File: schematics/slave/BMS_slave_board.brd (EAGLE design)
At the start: 75.9 x 50.8 mm, 73 parts, among them IC1 78L05F, IC2 ATTINY87/167AUTOMOTIVESOIC, IC3 LT1021S, IC4 78L05F, J1 AVR_SPI_PRG_6NS, Q1 BSS123, Q2 BSS123, Q3 BSS123, Q4 BSS123, U1 LMV324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

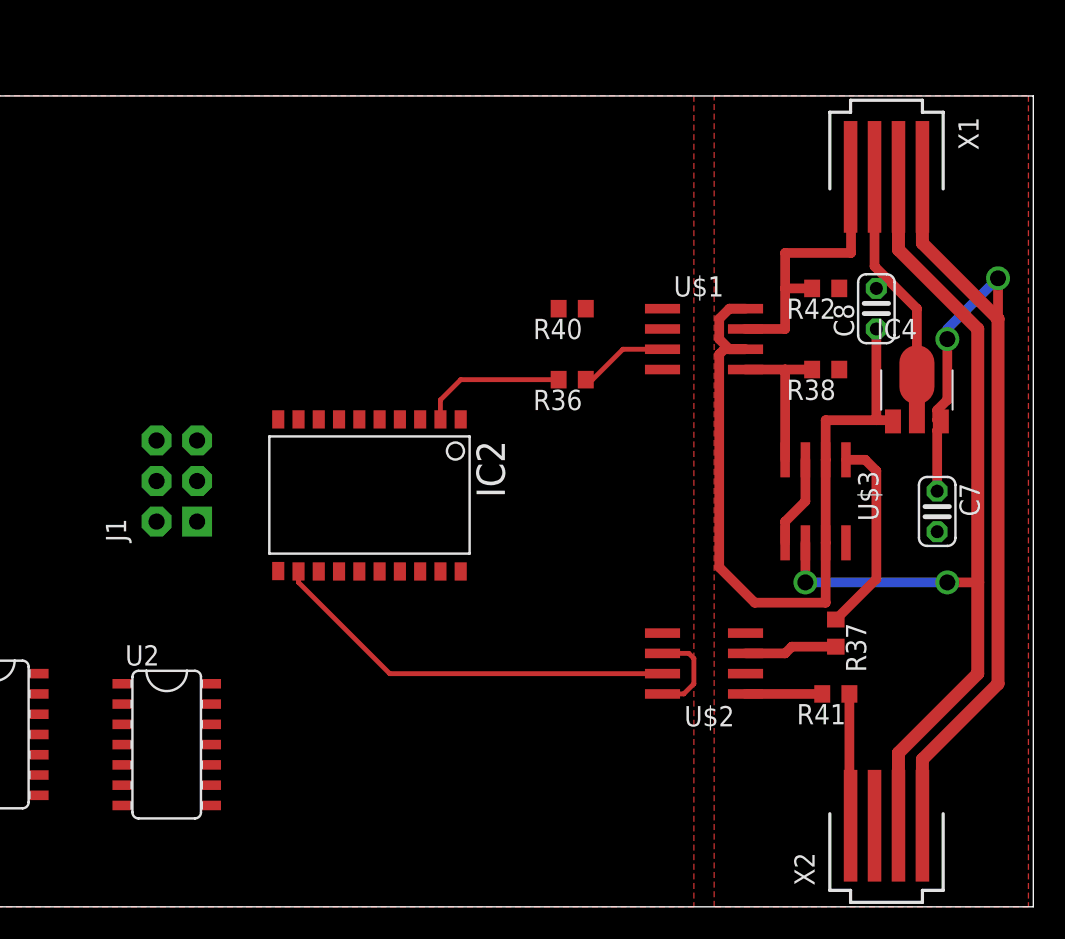
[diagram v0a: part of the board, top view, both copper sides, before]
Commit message: worked on ground plane and power pour
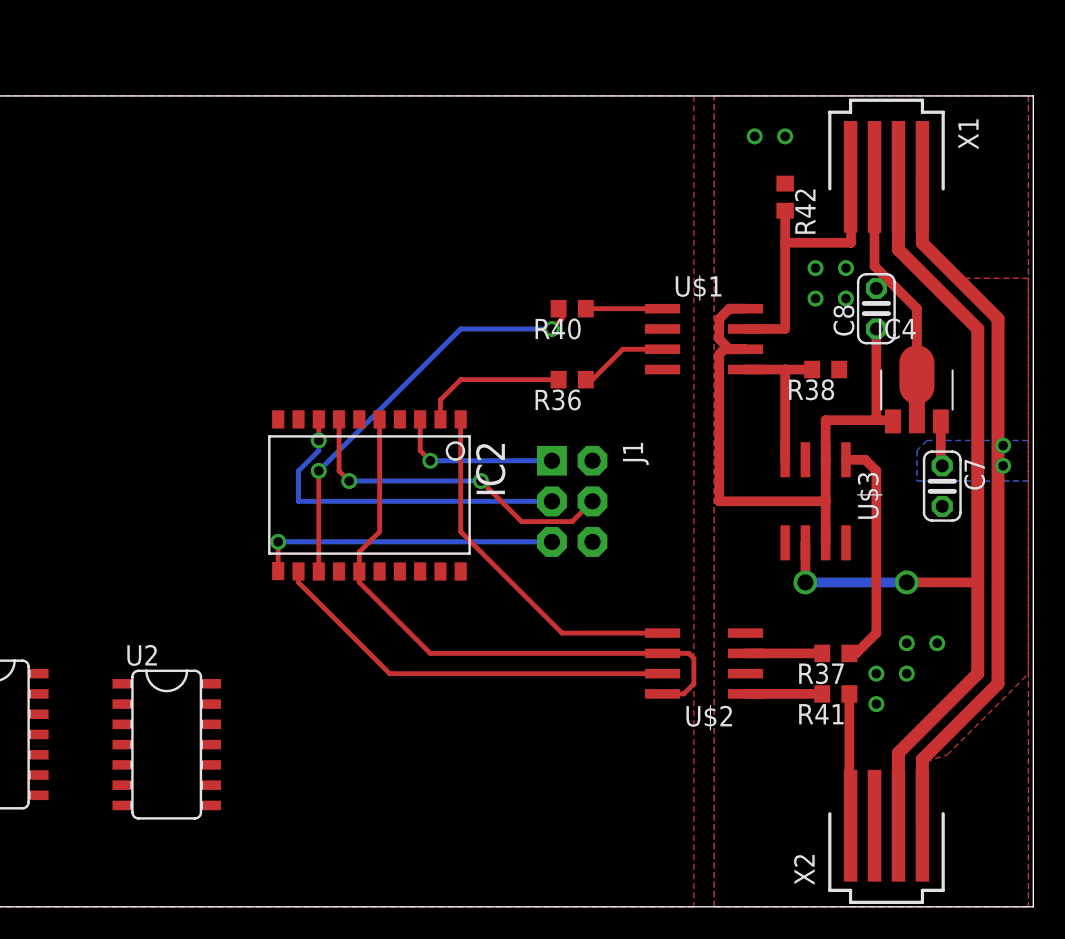
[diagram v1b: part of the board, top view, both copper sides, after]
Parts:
- moved J1 24.8 mm to (47.0, 25.4), turned to 270 degrees
- moved R42 6.25 mm to (60.3, 44.5), turned to 270 degrees
- moved C7 1.62 mm to (70.2, 26.4)
- moved R37 1.27 mm to (63.5, 15.9), turned to 180 degrees
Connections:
- net GND renamed IOGND
- net +3V3: no longer C2.1, IC1.1, IC3.2, J1.2
- net +5V: now also C2.1, IC1.1, IC3.2, J1.2
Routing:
- net +5V: track 5.91 -> 37.5 mm
- net ENUMO: track 0.00 -> 26.4 mm, vias 0 -> 2
- net RX: track 0.00 -> 22.3 mm
- net READ4: track 0.00 -> 21.5 mm, vias 0 -> 1
- net READ3: track 0.00 -> 20.9 mm, vias 0 -> 2
- net RESET: track 0.00 -> 19.0 mm, vias 0 -> 1
- net +12V: track 62.2 -> 47.4 mm
- net READ1: track 0.00 -> 10.5 mm, vias 0 -> 1
- net VCC: track 49.2 -> 40.4 mm
- net GNDIO: track 21.9 -> 16.2 mm, vias 0 -> 11
- net N$25: track 0.00 -> 4.80 mm
- net RXD: track 12.6 -> 14.6 mm
- net N$29: track 5.83 -> 4.80 mm
- added copper zone on layer 1, net +12V
- added copper zone on layer 16, net +12V
- added copper zone on layer 16, net GNDIO

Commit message: more work on the ground plane
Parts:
- moved C7 14.3 mm to (73.3, 40.3), turned to 90 degrees
- moved IC4 1.80 mm to (67.3, 33.7)
- moved C8 1.42 mm to (64.8, 38.1)
- moved R38 1.14 mm to (62.2, 34.6), turned to 270 degrees
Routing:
- net GNDIO: track 16.2 -> 0.00 mm, vias 11 -> 9
- net RESET: track 19.0 -> 20.7 mm
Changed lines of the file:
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@@
 <element name="R36" library="rcl" package="R0603" value="" x="46.99" y="33.02" rot="R180"/>
 <element name="R37" library="rcl" package="R0603" value="" x="63.5" y="15.875" rot="R180"/>
-<element name="R38" library="rcl" package="R0603" value="" x="62.865" y="33.655" rot="R180"/>
+<element name="R38" library="rcl" package="R0603" value="" x="62.23" y="34.6075" rot="R270"/>
 <element name="R39" library="rcl" package="R0603" value="" x="-41.91" y="64.77"/>
 <element name="U$3" library="EVT-Eagle-Library" package="SO08" value="TPIC1021" x="62.23" y="25.4" rot="R180"/>
-<element name="C7" library="resistor" package="C025-024X044" value="" x="70.1675" y="26.3525" rot="R270"/>
-<element name="C8" library="resistor" package="C025-024X044" value="" x="66.04" y="37.465" rot="R90"/>
-<element name="IC4" library="linear" package="SOT89" value="78L05F" x="68.58" y="32.385"/>
+<element name="C7" library="resistor" package="C025-024X044" value="" x="73.3425" y="40.3225" rot="R90"/>
+<element name="C8" library="resistor" package="C025-024X044" value="" x="64.77" y="38.1" rot="R90"/>
+<element name="IC4" library="linear" package="SOT89" value="78L05F" x="67.31" y="33.655"/>
 <element name="JP1" library="jumper" package="JP1" value="" x="-27.94" y="46.99"/>
 <element name="R40" library="rcl" package="R0603" value="" x="46.99" y="37.465" rot="R180"/>
@@
 <contactref element="R1" pad="2"/>
 <contactref element="IC2" pad="11"/>
-<wire x1="45.72" y1="22.86" x2="28.575" y2="22.86" width="0.3048" layer="16"/>
-<via x="28.575" y="22.86" extent="1-16" drill="0.6"/>
-<wire x1="28.575" y1="22.86" x2="28.575" y2="21.0312" width="0.3048" layer="1"/>
-<wire x1="28.575" y1="22.86" x2="-19.47" y2="68.58" width="0" layer="19" extent="1-16"/>
+<via x="28.575" y="19.05" extent="1-16" drill="0.6"/>
+<wire x1="28.575" y1="19.05" x2="28.575" y2="21.0312" width="0.3048" layer="1"/>
+<wire x1="45.72" y1="22.86" x2="43.815" y2="22.86" width="0.4064" layer="16"/>
+<wire x1="43.815" y1="22.86" x2="40.005" y2="19.05" width="0.4064" layer="16"/>
+<wire x1="40.005" y1="19.05" x2="28.575" y2="19.05" width="0.4064" layer="16"/>
+<wire x1="28.575" y1="21.0312" x2="-19.47" y2="68.58" width="0" layer="19" extent="1-1"/>
 </signal>
 <signal name="VREF">
@@
 <contactref element="C2" pad="1"/>
 <contactref element="IC1" pad="1"/>
+<wire x1="52.645" y1="15.875" x2="48.26" y2="27.94" width="0" layer="19" extent="1-1"/>
 <wire x1="-21.17" y1="68.58" x2="34.925" y2="30.5308" width="0" layer="19" extent="1-1"/>
 <wire x1="-57.15" y1="44.45" x2="-21.17" y2="68.58" width="0" layer="19" extent="1-1"/>
 <wire x1="-61.595" y1="25.34" x2="-57.15" y2="44.45" width="0" layer="19" extent="1-1"/>
 <wire x1="-47.219" y1="27.229" x2="-61.595" y2="25.34" width="0" layer="19" extent="1-1"/>
-<wire x1="52.645" y1="15.875" x2="48.26" y2="27.94" width="0" layer="19" extent="1-1"/>
 </signal>
 <signal name="TX">
@@
 <contactref element="U$2" pad="4"/>
 <contactref element="U$2" pad="2"/>
-<wire x1="65.925" y1="45.72" x2="65.925" y2="40.12" width="0.6096" layer="1"/>
-<wire x1="65.925" y1="40.12" x2="68.58" y2="37.465" width="0.6096" layer="1"/>
-<wire x1="68.58" y1="37.465" x2="68.58" y2="33.325" width="0.6096" layer="1"/>
-<wire x1="68.58" y1="30.658" x2="68.58" y2="33.325" width="0.6096" layer="1"/>
 <polygon width="0.6096" layer="1" isolate="0.4064" orphans="yes" rank="2">
 <vertex x="75.565" y="50.8"/>
@@
 <via x="62.23" y="40.005" extent="1-16" drill="0.6"/>
 <via x="62.23" y="38.1" extent="1-16" drill="0.6"/>
-<via x="64.135" y="40.005" extent="1-16" drill="0.6"/>
+<via x="67.945" y="14.605" extent="1-16" drill="0.6"/>
+<via x="67.945" y="18.415" extent="1-16" drill="0.6"/>
 <via x="67.945" y="16.51" extent="1-16" drill="0.6"/>
-<via x="69.85" y="16.51" extent="1-16" drill="0.6"/>
-<via x="67.945" y="14.605" extent="1-16" drill="0.6"/>
-<via x="58.42" y="48.26" extent="1-16" drill="0.6"/>
-<via x="60.325" y="48.26" extent="1-16" drill="0.6"/>
-<via x="64.135" y="38.1" extent="1-16" drill="0.6"/>
+<via x="57.785" y="45.4025" extent="1-16" drill="0.6"/>
+<via x="60.325" y="47.9425" extent="1-16" drill="0.6"/>
 <via x="66.04" y="14.605" extent="1-16" drill="0.6"/>
 <via x="66.04" y="12.7" extent="1-16" drill="0.6"/>
@@
 <wire x1="68.925" y1="9.235" x2="73.66" y2="13.97" width="0.8128" layer="1"/>
 <wire x1="73.66" y1="13.97" x2="73.66" y2="36.83" width="0.8128" layer="1"/>
-<polygon width="0.6096" layer="16" isolate="0.4064">
-<vertex x="75.565" y="29.21"/>
-<vertex x="69.215" y="29.21"/>
-<vertex x="68.58" y="28.575"/>
-<vertex x="68.58" y="26.67"/>
-<vertex x="75.565" y="26.67"/>
-</polygon>
-<wire x1="70.079" y1="30.404" x2="70.079" y2="27.711" width="0.6096" layer="1"/>
-<wire x1="70.079" y1="27.711" x2="70.1675" y2="27.6225" width="0.6096" layer="1"/>
 <polygon width="0.6096" layer="1" isolate="0.4064">
 <vertex x="75.565" y="39.37"/>
@@
 <vertex x="75.565" y="14.605"/>
 </polygon>
-<via x="73.9775" y="28.8925" extent="1-16" drill="0.6"/>
-<via x="73.9775" y="27.6225" extent="1-16" drill="0.6"/>
+<wire x1="68.809" y1="31.674" x2="68.809" y2="30.709" width="0.6096" layer="1"/>
+<wire x1="68.809" y1="30.709" x2="67.31" y2="29.21" width="0.6096" layer="1"/>
+<via x="67.31" y="29.21" extent="1-16" drill="0.6"/>
+<polygon width="0.6096" layer="16">
+<vertex x="75.565" y="29.845"/>
+<vertex x="66.675" y="29.845"/>
+<vertex x="66.675" y="28.575"/>
+<vertex x="75.565" y="28.575"/>
+</polygon>
+<via x="73.9775" y="29.21" extent="1-16" drill="0.6"/>
 </signal>
 <signal name="VCC">
@@
 <wire x1="57.845" y1="34.925" x2="56.515" y2="34.925" width="0.6096" layer="1"/>
 <wire x1="56.515" y1="34.925" x2="56.1975" y2="34.6075" width="0.6096" layer="1"/>
-<wire x1="62.865" y1="30.48" x2="66.04" y2="30.48" width="0.6096" layer="1"/>
-<wire x1="66.04" y1="30.48" x2="67.005" y2="30.48" width="0.6096" layer="1"/>
-<wire x1="67.005" y1="30.48" x2="67.081" y2="30.404" width="0.6096" layer="1"/>
-<wire x1="66.04" y1="36.195" x2="66.04" y2="30.48" width="0.6096" layer="1"/>
 <wire x1="62.865" y1="28" x2="62.865" y2="25.4" width="0.6096" layer="1"/>
 <wire x1="62.865" y1="25.4" x2="62.865" y2="22.8" width="0.6096" layer="1"/>
-<wire x1="62.865" y1="30.48" x2="62.865" y2="28" width="0.6096" layer="1"/>
 <wire x1="62.865" y1="25.4" x2="56.1975" y2="25.4" width="0.6096" layer="1"/>
 <wire x1="56.1975" y1="25.4" x2="56.1975" y2="34.6075" width="0.6096" layer="1"/>
+<wire x1="65.811" y1="31.674" x2="64.694" y2="31.674" width="0.6096" layer="1"/>
+<wire x1="64.694" y1="31.674" x2="64.694" y2="36.754" width="0.6096" layer="1"/>
+<wire x1="64.694" y1="36.754" x2="64.77" y2="36.83" width="0.6096" layer="1"/>
+<wire x1="62.865" y1="28" x2="62.865" y2="29.21" width="0.6096" layer="1"/>
+<wire x1="62.865" y1="29.21" x2="63.5" y2="29.845" width="0.6096" layer="1"/>
+<wire x1="63.5" y1="29.845" x2="65.7225" y2="29.845" width="0.6096" layer="1"/>
+<wire x1="65.7225" y1="29.845" x2="65.7225" y2="31.5855" width="0.6096" layer="1"/>
+<wire x1="65.7225" y1="31.5855" x2="65.811" y2="31.674" width="0.6096" layer="1"/>
 </signal>
 <signal name="TXD">
@@
 <wire x1="57.845" y1="33.655" x2="60.325" y2="33.655" width="0.6096" layer="1"/>
 <wire x1="60.325" y1="33.655" x2="60.325" y2="28" width="0.6096" layer="1"/>
-<wire x1="62.015" y1="33.655" x2="60.325" y2="33.655" width="0.6096" layer="1"/>
+<wire x1="60.4275" y1="33.5525" x2="60.325" y2="33.655" width="0.6096" layer="1"/>
+<wire x1="60.4275" y1="33.5525" x2="62.025" y2="33.5525" width="0.6096" layer="1"/>
+<wire x1="62.025" y1="33.5525" x2="62.23" y2="33.7575" width="0.6096" layer="1"/>
 </signal>
 <signal name="LIN">
@@
 <wire x1="67.425" y1="5.08" x2="67.425" y2="9.64" width="0.8128" layer="1"/>
 <wire x1="67.425" y1="9.64" x2="72.39" y2="14.605" width="0.8128" layer="1"/>
-<wire x1="67.945" y1="20.32" x2="72.39" y2="20.32" width="0.6096" layer="1"/>
-<wire x1="61.595" y1="20.32" x2="67.945" y2="20.32" width="0.6096" layer="16"/>
+<wire x1="70.485" y1="20.32" x2="72.39" y2="20.32" width="0.6096" layer="1"/>
+<wire x1="61.595" y1="20.32" x2="70.485" y2="20.32" width="0.6096" layer="16"/>
 <wire x1="61.595" y1="22.8" x2="61.595" y2="20.32" width="0.6096" layer="1"/>
-<via x="67.945" y="20.32" extent="1-16" drill="1"/>
+<via x="70.485" y="20.32" extent="1-16" drill="1"/>
 <via x="61.595" y="20.32" extent="1-16" drill="1"/>
 </signal>
